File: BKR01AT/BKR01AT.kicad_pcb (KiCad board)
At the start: 2 copper layers, 60 x 60 mm, 44 parts, among them J1 Conn_02x03_Odd_Even, SW1 SW_Push, SW2 SW_Push, SW3 SW_Push, U1 LIS2DHTR, Y1 32MHz, Y2 32.768kHz

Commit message: PCB: trilhas
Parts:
- moved C2 39.6 mm to (144.7, 71.3), turned to 180 degrees
- moved BT1 36.9 mm to (160.3, 71.3)
- moved R3 29.1 mm to (129.9, 102.6), turned to 90 degrees
- moved D3 23.8 mm to (132.2, 103.1), turned to 180 degrees
- moved R2 20.7 mm to (130.0, 99.4), turned to 90 degrees
- moved C17 15.9 mm to (153.4, 86.3), turned to 180 degrees
- moved D2 15.6 mm to (132.2, 99.9), turned to 180 degrees
- moved L1 15.1 mm to (145.5, 83.3), turned to 270 degrees
- moved R1 13.7 mm to (129.9, 96.3), turned to 90 degrees
- moved C16 13.4 mm to (153.4, 85.1), turned to 180 degrees
- moved C7 11.9 mm to (152.5, 90.2)
- moved C15 11.9 mm to (168.7, 91.9), turned to 270 degrees
- moved AE1 11.5 mm to (170.1, 86.7)
- moved C4 9.91 mm to (144.0, 87.9), turned to 180 degrees
- moved C6 9.87 mm to (142.6, 90.2), turned to 90 degrees
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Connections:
- MCU1 pad 17: b_F1 -> b_RST
- MCU1 pad 18: b_F2 -> b_F1
- MCU1 pad 19: b_RST -> b_F2
- MCU1 pad 37: ac_INT1 -> ac_INT2
- MCU1 pad 38: ac_INT2 -> ac_INT1
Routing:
- net b_F2: track 0.00 -> 28.7 mm
- net tag_RST: track 0.00 -> 27.2 mm
- net tag_SWDIO: track 0.00 -> 24.5 mm, vias 0 -> 2
- net Net-(C13-Pad1): track 0.00 -> 22.0 mm
- net tag_SWDCLK: track 0.00 -> 21.6 mm
- net b_F1: track 0.00 -> 19.2 mm
- net b_RST: track 0.00 -> 18.5 mm
- net led_TEMP: track 0.00 -> 17.9 mm
- net led_ON_OFF: track 0.00 -> 17.1 mm
- net led_VIB: track 0.00 -> 16.2 mm
- net Net-(C12-Pad2): track 0.00 -> 14.5 mm
- net Net-(C10-Pad2): track 0.00 -> 14.0 mm
- net Net-(C8-Pad2): track 0.00 -> 13.4 mm
- net Net-(C5-Pad2): track 0.00 -> 11.7 mm
- net Net-(C11-Pad1): track 0.00 -> 11.4 mm
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
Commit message: PCB
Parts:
- added REF**: KiCad-Logo2_5mm_SilkScreen, Symbol:KiCad-Logo2_5mm_SilkScreen, B.Cu at (151.1, 65.7)
- moved BT1 1.69 mm to (161.0, 69.8)
- moved H1 1.02 mm to (124.6, 63.7)
- moved FID2 0.96 mm to (122.7, 116.2)
- moved H2 0.60 mm to (174.3, 114.0)
- moved FID1 0.38 mm to (176.7, 61.2)
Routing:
- added copper zone on B.Cu, net Earth

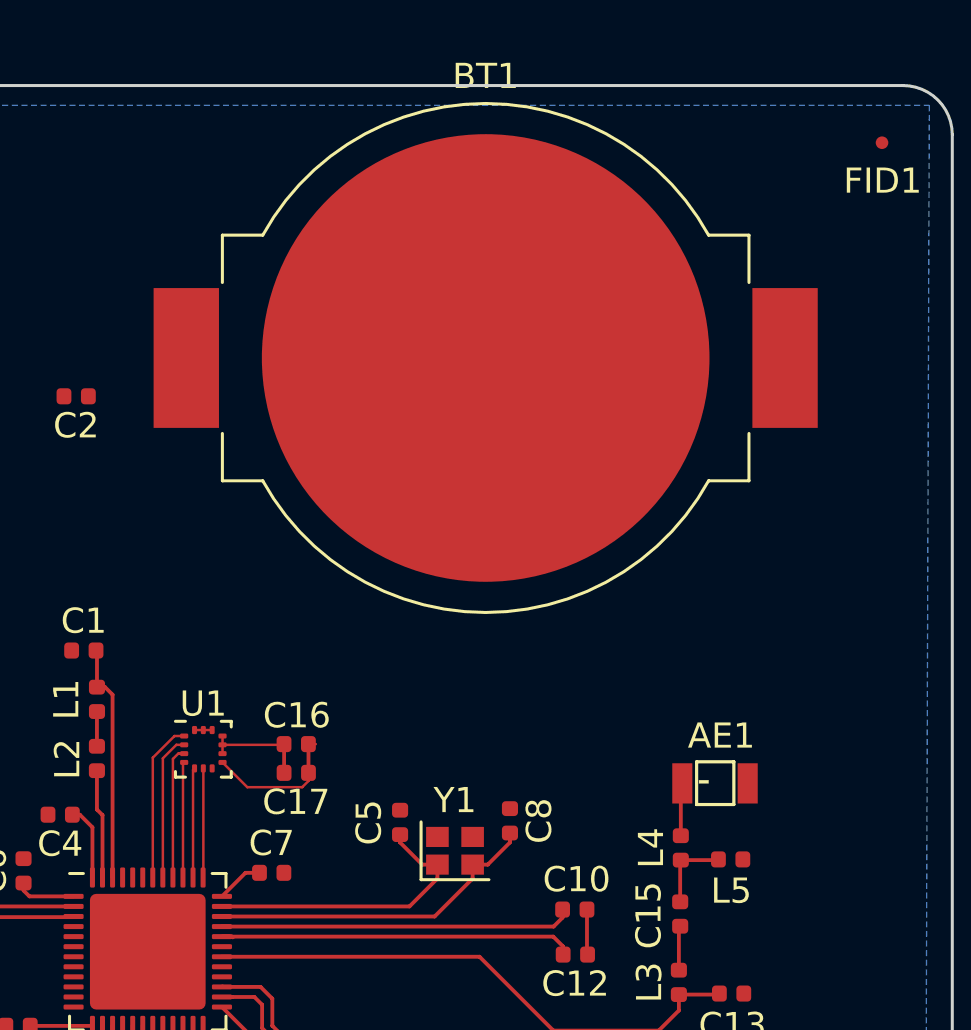
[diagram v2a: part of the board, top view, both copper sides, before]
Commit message: PCB
clearence
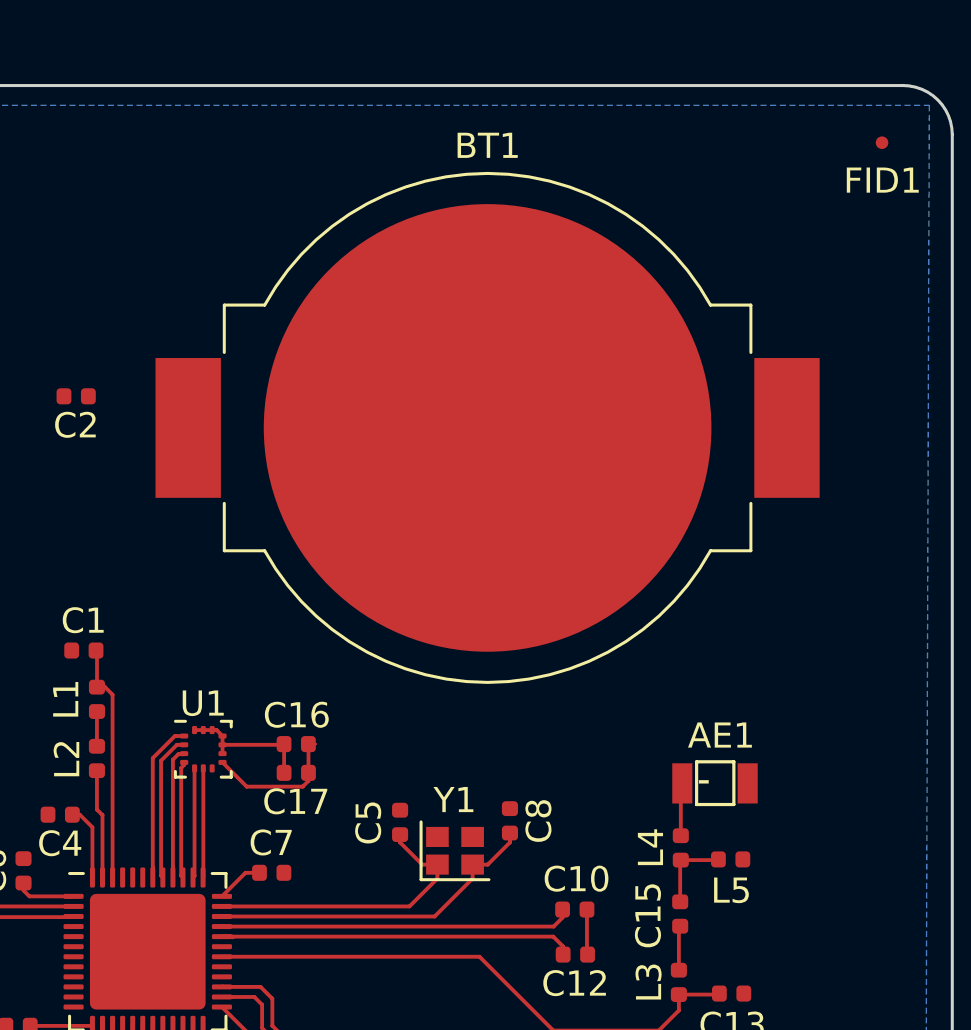
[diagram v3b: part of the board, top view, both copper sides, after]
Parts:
- moved BT1 2.78 mm to (161.0, 72.6)
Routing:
- net Earth: track 9.33 -> 9.85 mm
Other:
- net class Default: clearance 0.2 -> 0.1524
- rule trace_clearance: 0.2 -> 0.1524
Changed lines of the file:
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@@
     (thickness 1.6)
     (drawings 9)
-    (tracks 184)
+    (tracks 192)
     (zones 0)
     (modules 45)
@@
   )
   (setup
-    (last_trace_width 0.1524)
-    (user_trace_width 0.1)
+    (last_trace_width 0.3048)
     (user_trace_width 0.1524)
     (user_trace_width 0.3048)
-    (trace_clearance 0.2)
+    (trace_clearance 0.1524)
     (zone_clearance 0.508)
     (zone_45_only no)
@@
   (net 54 "Net-(U1-Pad7)")
   (net_class Default "Esta é a classe de rede padrão."
-    (clearance 0.2)
+    (clearance 0.1524)
     (trace_width 0.25)
     (via_dia 0.8)
@@
   )
   (module Battery:BatteryHolder_MPD_BC2003_1x2032 (layer F.Cu)
-    (at 160.9598 69.7738)
+    (at 161.036 72.5551)
     (descr http://www.memoryprotectiondevices.com/datasheets/BC-2003-datasheet.pdf)
     (tags "BC2003 CR2032 2032 Battery Holder")
@@
   (segment (start 153.9137 85.1305) (end 153.9113 85.1281) (width 0.1524) (layer F.Cu) (net 2))
   (segment (start 153.9137 86.2711) (end 153.9137 85.1305) (width 0.1524) (layer F.Cu) (net 2))
-  (segment (start 150.4955 85.8563) (end 151.48031 86.84111) (width 0.1) (layer F.Cu) (net 2))
-  (segment (start 153.9137 86.5911) (end 153.9137 86.2711) (width 0.1) (layer F.Cu) (net 2))
-  (segment (start 153.66369 86.84111) (end 153.9137 86.5911) (width 0.1) (layer F.Cu) (net 2))
-  (segment (start 151.48031 86.84111) (end 153.66369 86.84111) (width 0.1) (layer F.Cu) (net 2))
   (segment (start 153.9113 85.1281) (end 154.2063 85.1281) (width 0.1) (layer F.Cu) (net 2))
   (segment (start 151.4101 90.2462) (end 151.9658 90.2462) (width 0.1524) (layer F.Cu) (net 2))
   (segment (start 150.4732 91.1831) (end 151.4101 90.2462) (width 0.1524) (layer F.Cu) (net 2))
+  (segment (start 151.45891 86.81971) (end 153.68509 86.81971) (width 0.1524) (layer F.Cu) (net 2))
+  (segment (start 153.9137 86.5911) (end 153.9137 86.2711) (width 0.1524) (layer F.Cu) (net 2))
+  (segment (start 153.68509 86.81971) (end 153.9137 86.5911) (width 0.1524) (layer F.Cu) (net 2))
+  (segment (start 150.4955 85.8563) (end 151.45891 86.81971) (width 0.1524) (layer F.Cu) (net 2))
   (segment (start 133.1166 90.6447) (end 133.1214 90.6399) (width 0.1524) (layer F.Cu) (net 3))
   (segment (start 133.1166 93.1672) (end 133.1166 90.6447) (width 0.1524) (layer F.Cu) (net 3))
-  (segment (start 149.383 84.5688) (end 149.733 84.5688) (width 0.1) (layer F.Cu) (net 3))
-  (segment (start 149.733 84.5688) (end 150.083 84.5688) (width 0.1) (layer F.Cu) (net 3))
-  (segment (start 150.4955 84.8063) (end 150.4955 85.1563) (width 0.1) (layer F.Cu) (net 3))
-  (segment (start 150.4955 85.1563) (end 150.4955 85.5063) (width 0.1) (layer F.Cu) (net 3))
-  (segment (start 152.9131 85.1563) (end 152.9413 85.1281) (width 0.1) (layer F.Cu) (net 3))
-  (segment (start 150.4955 85.1563) (end 152.9131 85.1563) (width 0.1) (layer F.Cu) (net 3))
   (segment (start 152.9413 86.2687) (end 152.9437 86.2711) (width 0.1) (layer F.Cu) (net 3))
   (segment (start 152.9437 85.1305) (end 152.9413 85.1281) (width 0.1524) (layer F.Cu) (net 3))
@@
   (segment (start 164.9881 93.4744) (end 165.0111 93.4974) (width 0.1524) (layer F.Cu) (net 3))
   (segment (start 164.9881 91.7067) (end 164.9881 93.4744) (width 0.1524) (layer F.Cu) (net 3))
+  (segment (start 152.9131 85.1563) (end 152.9413 85.1281) (width 0.1524) (layer F.Cu) (net 3))
+  (segment (start 150.4955 85.1563) (end 152.9131 85.1563) (width 0.1524) (layer F.Cu) (net 3))
+  (segment (start 150.4955 85.5063) (end 150.4955 85.1563) (width 0.1524) (layer F.Cu) (net 3))
+  (segment (start 150.4955 85.1563) (end 150.4955 84.8063) (width 0.1524) (layer F.Cu) (net 3))
+  (segment (start 150.083 84.5688) (end 149.733 84.5688) (width 0.1524) (layer F.Cu) (net 3))
+  (segment (start 149.733 84.5688) (end 149.383 84.5688) (width 0.1524) (layer F.Cu) (net 3))
+  (segment (start 150.258 84.5688) (end 150.4955 84.8063) (width 0.1524) (layer F.Cu) (net 3))
+  (segment (start 150.083 84.5688) (end 150.258 84.5688) (width 0.1524) (layer F.Cu) (net 3))
   (segment (start 145.8239 82.8627) (end 145.5039 82.8627) (width 0.1524) (layer F.Cu) (net 4))
   (segment (start 146.1232 83.162) (end 145.8239 82.8627) (width 0.1524) (layer F.Cu) (net 4))
@@
   (segment (start 145.5015 87.7292) (end 145.5015 86.1846) (width 0.1524) (layer F.Cu) (net 26))
   (segment (start 145.7232 87.9509) (end 145.5015 87.7292) (width 0.1524) (layer F.Cu) (net 26))
-  (segment (start 148.585164 84.8063) (end 148.9705 84.8063) (width 0.1) (layer F.Cu) (net 29))
-  (segment (start 147.7232 90.4331) (end 147.7232 85.668264) (width 0.1) (layer F.Cu) (net 29))
-  (segment (start 147.7232 85.668264) (end 148.585164 84.8063) (width 0.1) (layer F.Cu) (net 29))
-  (segment (start 148.659452 85.15629) (end 148.8059 85.15629) (width 0.1) (layer F.Cu) (net 30))
-  (segment (start 148.1232 90.4331) (end 148.1232 85.692542) (width 0.1) (layer F.Cu) (net 30))
-  (segment (start 148.1232 85.692542) (end 148.659452 85.15629) (width 0.1) (layer F.Cu) (net 30))
-  (segment (start 148.808 85.5063) (end 148.9705 85.5063) (width 0.1) (layer F.Cu) (net 31))
-  (segment (start 148.73372 85.5063) (end 148.808 85.5063) (width 0.1) (layer F.Cu) (net 31))
-  (segment (start 148.5232 85.71682) (end 148.73372 85.5063) (width 0.1) (layer F.Cu) (net 31))
-  (segment (start 148.5232 90.4331) (end 148.5232 85.71682) (width 0.1) (layer F.Cu) (net 31))
-  (segment (start 148.9232 85.9036) (end 148.9705 85.8563) (width 0.1) (layer F.Cu) (net 32))
-  (segment (start 148.9232 90.4331) (end 148.9232 85.9036) (width 0.1) (layer F.Cu) (net 32))
-  (segment (start 149.733 90.4233) (end 149.7232 90.4331) (width 0.1) (layer F.Cu) (net 33))
-  (segment (start 149.733 86.0938) (end 149.733 90.4233) (width 0.1) (layer F.Cu) (net 33))
-  (segment (start 149.3232 86.1536) (end 149.383 86.0938) (width 0.1) (layer F.Cu) (net 34))
-  (segment (start 149.3232 90.4331) (end 149.3232 86.1536) (width 0.1) (layer F.Cu) (net 34))
+  (segment (start 147.7232 90.0331) (end 147.7232 90.4331) (width 0.1524) (layer F.Cu) (net 29))
+  (segment (start 147.7232 85.684952) (end 147.7232 90.0331) (width 0.1524) (layer F.Cu) (net 29))
+  (segment (start 148.601852 84.8063) (end 147.7232 85.684952) (width 0.1524) (layer F.Cu) (net 29))
+  (segment (start 148.9705 84.8063) (end 148.601852 84.8063) (width 0.1524) (layer F.Cu) (net 29))
+  (segment (start 148.05181 90.36171) (end 148.1232 90.4331) (width 0.1524) (layer F.Cu) (net 30))
+  (segment (start 148.05181 85.787408) (end 148.05181 90.36171) (width 0.1524) (layer F.Cu) (net 30))
+  (segment (start 148.9705 85.1563) (end 148.682918 85.1563) (width 0.1524) (layer F.Cu) (net 30))
+  (segment (start 148.682918 85.1563) (end 148.05181 85.787408) (width 0.1524) (layer F.Cu) (net 30))
+  (segment (start 148.742594 85.52769) (end 148.5232 85.747084) (width 0.1524) (layer F.Cu) (net 31))
+  (segment (start 148.5232 90.0331) (end 148.5232 90.4331) (width 0.1524) (layer F.Cu) (net 31))
+  (segment (start 148.95141 85.52769) (end 148.742594 85.52769) (width 0.1524) (layer F.Cu) (net 31))
+  (segment (start 148.5232 85.747084) (end 148.5232 90.0331) (width 0.1524) (layer F.Cu) (net 31))
+  (segment (start 148.9705 85.5086) (end 148.95141 85.52769) (width 0.1524) (layer F.Cu) (net 31))
+  (segment (start 148.9705 85.5063) (end 148.9705 85.5086) (width 0.1524) (layer F.Cu) (net 31))
+  (segment (start 148.85181 90.36171) (end 148.9232 90.4331) (width 0.1524) (layer F.Cu) (net 32))
+  (segment (start 148.9705 85.8563) (end 148.9705 85.9563) (width 0.1524) (layer F.Cu) (net 32))
+  (segment (start 148.85181 86.07499) (end 148.85181 90.36171) (width 0.1524) (layer F.Cu) (net 32))
+  (segment (start 148.9705 85.9563) (end 148.85181 86.07499) (width 0.1524) (layer F.Cu) (net 32))
+  (segment (start 149.733 90.4233) (end 149.7232 90.4331) (width 0.1524) (layer F.Cu) (net 33))
+  (segment (start 149.733 86.0938) (end 149.733 90.4233) (width 0.1524) (layer F.Cu) (net 33))
+  (segment (start 149.383 90.3733) (end 149.3232 90.4331) (width 0.1524) (layer F.Cu) (net 34))
+  (segment (start 149.383 86.0938) (end 149.383 90.3733) (width 0.1524) (layer F.Cu) (net 34))
   (segment (start 137.863013 106.4895) (end 142.9488 106.4895) (width 0.1524) (layer F.Cu) (net 42))
   (segment (start 136.4488 106.4895) (end 137.863013 106.4895) (width 0.1524) (layer F.Cu) (net 42))

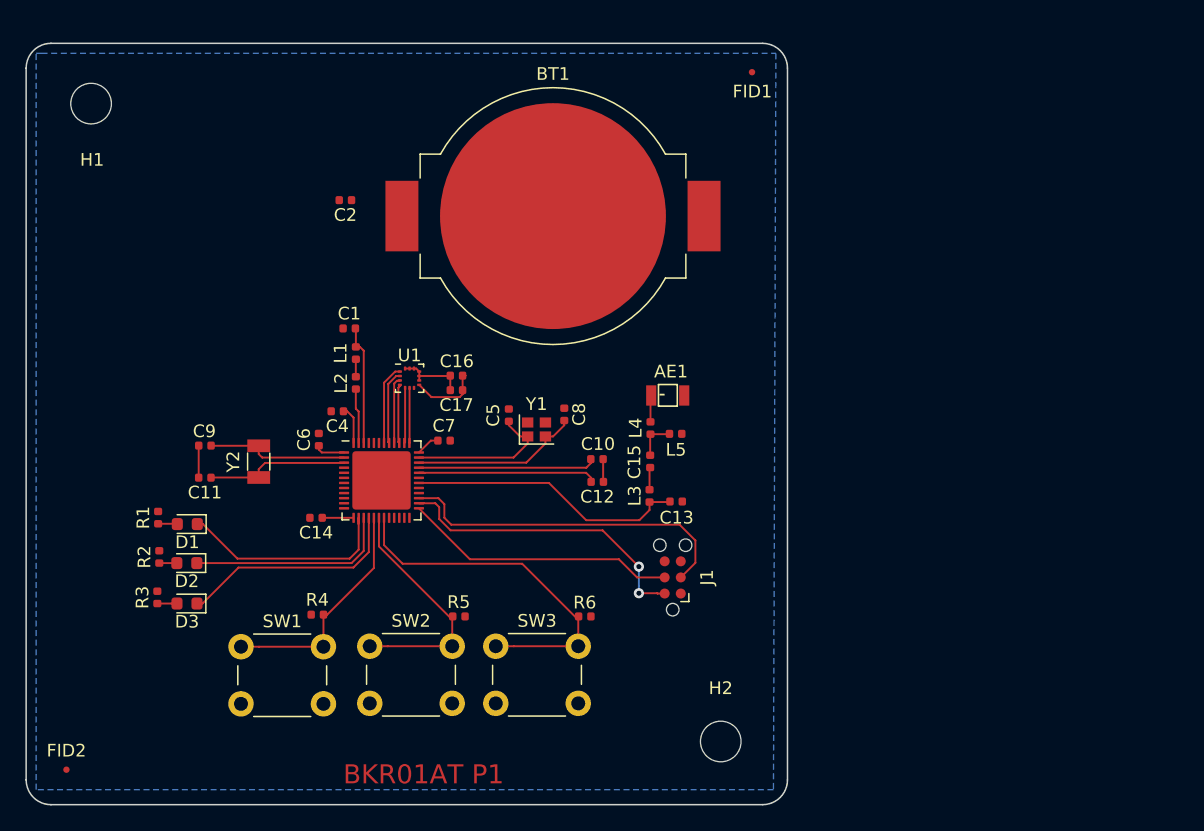
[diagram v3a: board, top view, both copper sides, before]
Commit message: PCB
trilhas de alimentação, shielding e stitching da antena
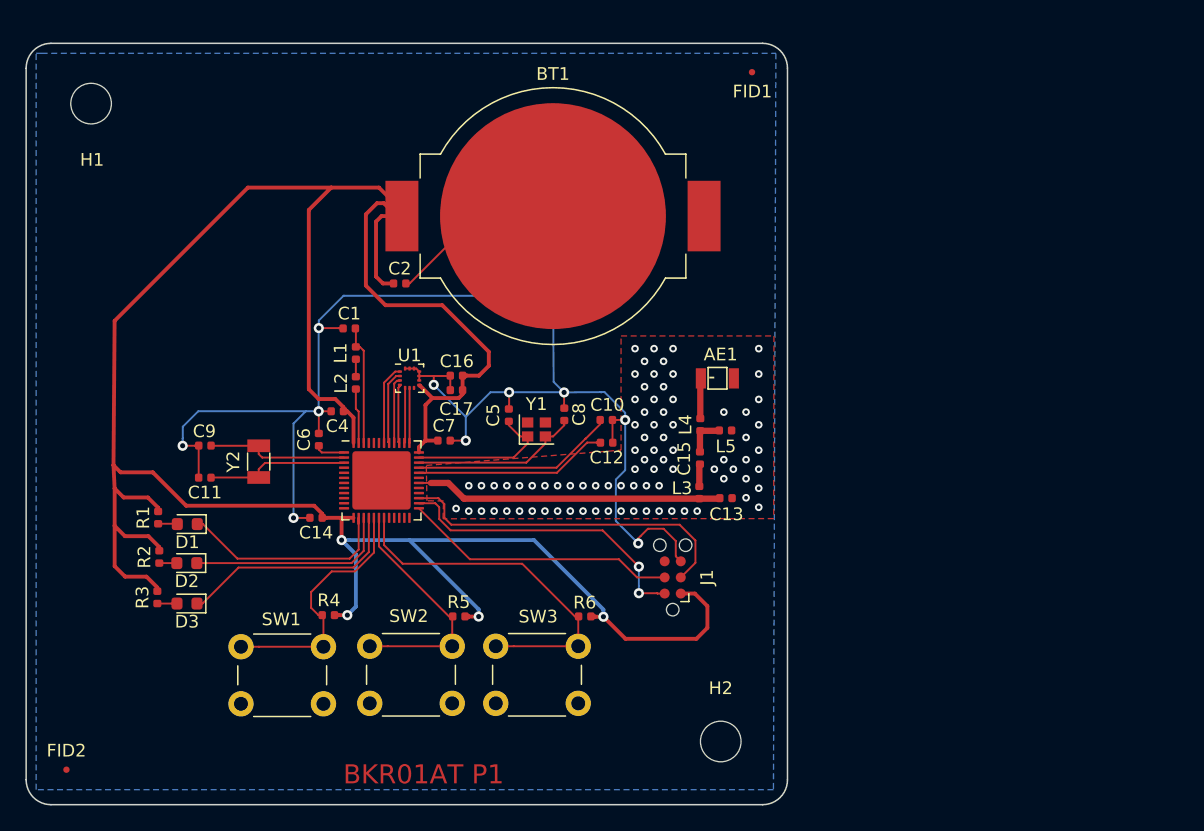
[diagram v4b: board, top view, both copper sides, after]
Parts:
- moved C2 7.84 mm to (149.0, 77.9), turned to 0 degrees
- moved AE1 4.14 mm to (174.0, 85.3)
- moved C15 3.93 mm to (172.6, 91.6)
- moved C13 3.93 mm to (174.7, 94.8)
- moved L3 3.93 mm to (172.6, 94.3)
- moved L4 3.93 mm to (172.6, 89.0)
- moved L5 3.93 mm to (174.6, 89.4)
- moved C10 3.17 mm to (165.2, 88.6)
- moved C12 3.17 mm to (165.3, 90.4)
- moved R4 0.87 mm to (143.3, 104.0), turned to 180 degrees
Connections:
- net Earth renamed GND
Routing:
- net VDD: track 13.0 -> 205.7 mm, vias 0 -> 4
- net GND: track 9.85 -> 137.9 mm, vias 0 -> 92
- net Net-(C13-Pad1): track 22.0 -> 24.6 mm
- net Net-(C10-Pad2): track 14.0 -> 16.0 mm
- net b_RST: track 18.5 -> 20.4 mm
- net Net-(AE1-Pad1): track 2.10 -> 3.18 mm
- net Net-(C12-Pad2): track 14.5 -> 15.3 mm
- added copper zone on F.Cu, net GND

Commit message: gerbers
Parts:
- removed REF**: KiCad-Logo2_5mm_SilkScreen, Symbol:KiCad-Logo2_5mm_SilkScreen
- added G***: LOGO, 2450AT18B100E:Arco_e_Flecha, F.Cu at (175.2, 63.2)
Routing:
- net VDD: track 205.7 -> 240.7 mm
- net GND: track 137.9 -> 156.0 mm, vias 92 -> 93
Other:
- rule trace_min: 0.1 -> 0

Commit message: corrigido o logo da empresa
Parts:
- removed the G*** at (175.2, 63.2)
- added G***: LOGO, 2450AT18B100E:logo, B.Cu at (152.0, 64.0)
